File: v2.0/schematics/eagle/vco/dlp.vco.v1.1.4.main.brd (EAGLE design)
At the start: 87.9 x 38.1 mm, 72 parts, among them IC1 TL074P, IC2 TL074P, IC3 TL074P, IC5 TL072P, Q1 2N4401, Q10 2N4401, Q2 2N4401, Q3 2N3417, Q4 2N3906, Q5 2N3417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

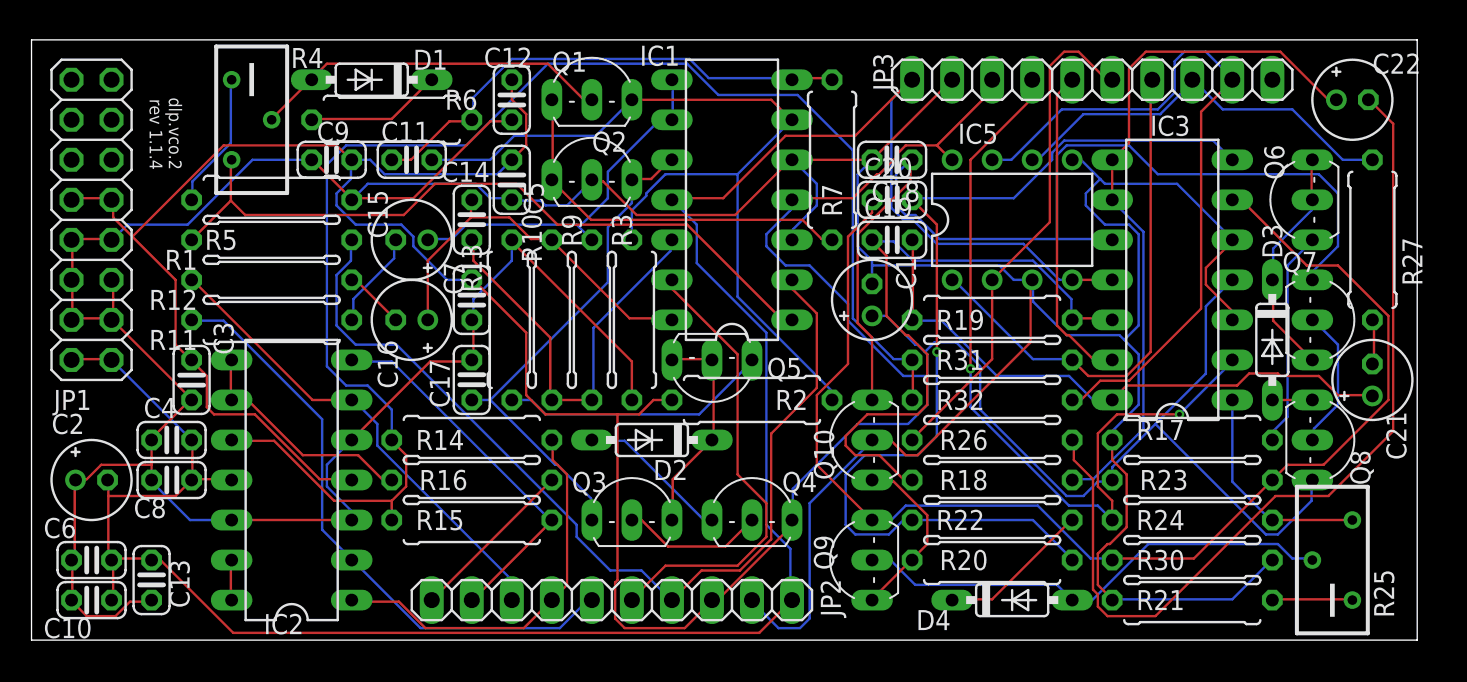
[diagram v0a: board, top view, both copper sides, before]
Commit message: Update component names on board layout Reverse cap polarity on v1.0 psu schem
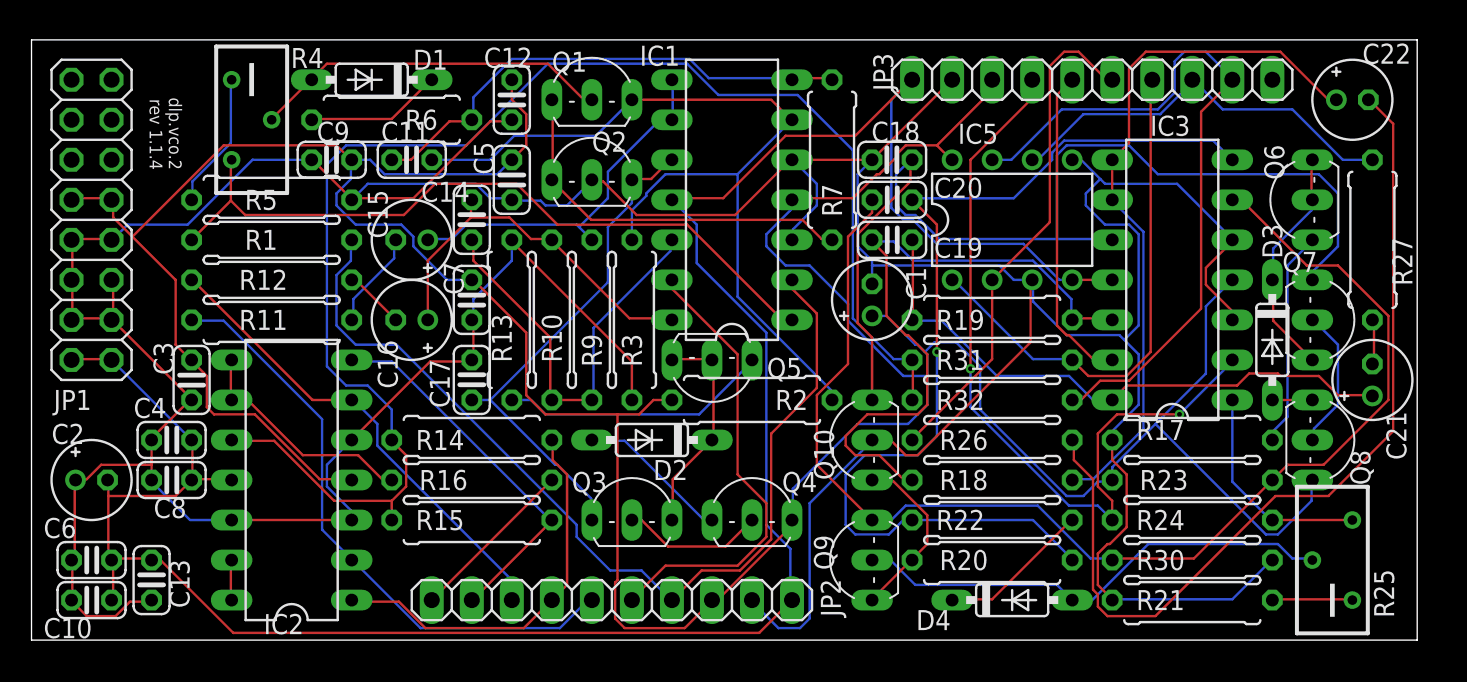
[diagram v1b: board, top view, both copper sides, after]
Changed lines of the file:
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@@
 </element>
 <element name="C5" library="_common" package="C025-024X044" value="0.1uF" x="30.48" y="29.21" smashed="yes" rot="R270">
-<attribute name="NAME" x="31.242" y="29.083" size="1.27" layer="25" ratio="10" rot="R270"/>
+<attribute name="NAME" x="28.067" y="31.623" size="1.27" layer="25" ratio="10" rot="R270"/>
 <attribute name="VALUE" x="27.813" y="30.988" size="1.27" layer="27" ratio="10" rot="R270"/>
 </element>
@@
 </element>
 <element name="C3" library="_common" package="C025-024X044" value="0.1uF" x="10.16" y="16.51" smashed="yes" rot="R270">
-<attribute name="NAME" x="11.557" y="20.193" size="1.27" layer="25" ratio="10" rot="R270"/>
+<attribute name="NAME" x="7.747" y="18.923" size="1.27" layer="25" ratio="10" rot="R270"/>
 <attribute name="VALUE" x="7.493" y="18.288" size="1.27" layer="27" ratio="10" rot="R270"/>
 </element>
 <element name="C1" library="_common" package="E2-5" value="10uF" x="53.34" y="21.59" smashed="yes" rot="R90">
-<attribute name="NAME" x="56.134" y="22.225" size="1.27" layer="25" ratio="10" rot="R90"/>
+<attribute name="NAME" x="56.769" y="21.59" size="1.27" layer="25" ratio="10" rot="R90"/>
 <attribute name="VALUE" x="55.499" y="24.13" size="1.27" layer="27" ratio="10" rot="R90"/>
 </element>
 <element name="C14" library="_common" package="C025-024X044" value="18pF" x="27.94" y="26.67" smashed="yes" rot="R90">
-<attribute name="NAME" x="29.083" y="30.353" size="1.27" layer="25" ratio="10" rot="R180"/>
+<attribute name="NAME" x="27.813" y="29.083" size="1.27" layer="25" ratio="10" rot="R180"/>
 <attribute name="VALUE" x="30.607" y="24.892" size="1.27" layer="27" ratio="10" rot="R90"/>
 </element>
@@
 </element>
 <element name="C8" library="_common" package="C025-024X044" value="0.1uF" x="8.89" y="10.16" smashed="yes">
-<attribute name="NAME" x="6.477" y="7.747" size="1.27" layer="25" ratio="10"/>
+<attribute name="NAME" x="7.747" y="7.747" size="1.27" layer="25" ratio="10"/>
 <attribute name="VALUE" x="7.112" y="7.493" size="1.27" layer="27" ratio="10"/>
 </element>
@@
 </element>
 <element name="C4" library="_common" package="C025-024X044" value="0.1uF" x="8.89" y="12.7" smashed="yes">
-<attribute name="NAME" x="7.112" y="14.097" size="1.27" layer="25" ratio="10"/>
+<attribute name="NAME" x="6.477" y="14.097" size="1.27" layer="25" ratio="10"/>
 <attribute name="VALUE" x="7.112" y="10.033" size="1.27" layer="27" ratio="10"/>
 </element>
 <element name="C2" library="_common" package="E2-5" value="10uF" x="3.81" y="10.16" smashed="yes">
-<attribute name="NAME" x="1.27" y="13.081" size="1.27" layer="25" ratio="10"/>
+<attribute name="NAME" x="1.27" y="12.446" size="1.27" layer="25" ratio="10"/>
 <attribute name="VALUE" x="6.35" y="8.001" size="1.27" layer="27" ratio="10"/>
 </element>
@@
 </element>
 <element name="R13" library="_common" package="0309/10" value="10K" x="30.48" y="20.32" smashed="yes" rot="R270">
-<attribute name="NAME" x="27.305" y="25.146" size="1.27" layer="25" ratio="10" rot="R270"/>
+<attribute name="NAME" x="29.21" y="20.701" size="1.27" layer="25" ratio="10" rot="R270"/>
 <attribute name="VALUE" x="29.7942" y="23.495" size="1.27" layer="27" ratio="10" rot="R270"/>
 </element>
@@
 </element>
 <element name="R1" library="_common" package="0309/10" value="2.2K" x="15.24" y="25.4" smashed="yes" rot="R180">
-<attribute name="NAME" x="10.541" y="24.765" size="1.27" layer="25" ratio="10" rot="R180"/>
+<attribute name="NAME" x="15.621" y="26.035" size="1.27" layer="25" ratio="10" rot="R180"/>
 <attribute name="VALUE" x="18.415" y="26.0858" size="1.27" layer="27" ratio="10" rot="R180"/>
 </element>
 <element name="R11" library="_common" package="0309/10" value="22K" x="15.24" y="20.32" smashed="yes" rot="R180">
-<attribute name="NAME" x="10.541" y="19.685" size="1.27" layer="25" ratio="10" rot="R180"/>
+<attribute name="NAME" x="16.256" y="20.955" size="1.27" layer="25" ratio="10" rot="R180"/>
 <attribute name="VALUE" x="18.415" y="21.0058" size="1.27" layer="27" ratio="10" rot="R180"/>
 </element>
 <element name="R12" library="_common" package="0309/10" value="22K" x="15.24" y="22.86" smashed="yes" rot="R180">
-<attribute name="NAME" x="10.541" y="22.225" size="1.27" layer="25" ratio="10" rot="R180"/>
+<attribute name="NAME" x="16.256" y="23.495" size="1.27" layer="25" ratio="10" rot="R180"/>
 <attribute name="VALUE" x="18.415" y="23.5458" size="1.27" layer="27" ratio="10" rot="R180"/>
 </element>
 <element name="R9" library="_common" package="0309/10" value="100K" x="35.56" y="20.32" smashed="yes" rot="R270">
-<attribute name="NAME" x="33.655" y="27.051" size="1.27" layer="25" ratio="10" rot="R270"/>
+<attribute name="NAME" x="34.925" y="19.431" size="1.27" layer="25" ratio="10" rot="R270"/>
 <attribute name="VALUE" x="34.8742" y="23.495" size="1.27" layer="27" ratio="10" rot="R270"/>
 </element>
 <element name="R10" library="_common" package="0309/10" value="3.3M" x="33.02" y="20.32" smashed="yes" rot="R270">
-<attribute name="NAME" x="31.115" y="27.051" size="1.27" layer="25" ratio="10" rot="R270"/>
+<attribute name="NAME" x="32.385" y="20.701" size="1.27" layer="25" ratio="10" rot="R270"/>
 <attribute name="VALUE" x="32.3342" y="23.495" size="1.27" layer="27" ratio="10" rot="R270"/>
 </element>
@@
 </element>
 <element name="R3" library="_common" package="0309/10" value="100K" x="38.1" y="20.32" smashed="yes" rot="R270">
-<attribute name="NAME" x="36.83" y="27.051" size="1.27" layer="25" ratio="10" rot="R270"/>
+<attribute name="NAME" x="37.465" y="19.431" size="1.27" layer="25" ratio="10" rot="R270"/>
 <attribute name="VALUE" x="37.4142" y="23.495" size="1.27" layer="27" ratio="10" rot="R270"/>
 </element>
@@
 </element>
 <element name="R5" library="_common" package="0309/10" value="390" x="15.24" y="27.94" smashed="yes" rot="R180">
-<attribute name="NAME" x="13.081" y="26.035" size="1.27" layer="25" ratio="10" rot="R180"/>
+<attribute name="NAME" x="15.621" y="28.575" size="1.27" layer="25" ratio="10" rot="R180"/>
 <attribute name="VALUE" x="18.415" y="28.6258" size="1.27" layer="27" ratio="10" rot="R180"/>
 </element>
 <element name="R6" library="_common" package="0309/10" value="220K" x="22.86" y="33.02" smashed="yes" rot="R180">
-<attribute name="NAME" x="28.321" y="34.925" size="1.27" layer="25" ratio="10" rot="R180"/>
+<attribute name="NAME" x="25.781" y="33.655" size="1.27" layer="25" ratio="10" rot="R180"/>
 <attribute name="VALUE" x="26.035" y="33.7058" size="1.27" layer="27" ratio="10" rot="R180"/>
 </element>
@@
 </element>
 <element name="C18" library="_common" package="C025-024X044" value="0.01uF" x="54.61" y="30.48" smashed="yes" rot="R180">
-<attribute name="NAME" x="56.388" y="29.083" size="1.27" layer="25" ratio="10" rot="R180"/>
+<attribute name="NAME" x="56.388" y="32.893" size="1.27" layer="25" ratio="10" rot="R180"/>
 <attribute name="VALUE" x="56.388" y="33.147" size="1.27" layer="27" ratio="10" rot="R180"/>
 </element>
@@
 </element>
 <element name="C19" library="_common" package="C025-024X044" value="18pF" x="54.61" y="25.4" smashed="yes">
-<attribute name="NAME" x="52.832" y="26.797" size="1.27" layer="25" ratio="10"/>
+<attribute name="NAME" x="57.277" y="24.257" size="1.27" layer="25" ratio="10"/>
 <attribute name="VALUE" x="52.832" y="22.733" size="1.27" layer="27" ratio="10"/>
 </element>
@@
 </element>
 <element name="C20" library="_common" package="C025-024X044" value="100pF" x="54.61" y="27.94" smashed="yes">
-<attribute name="NAME" x="52.832" y="29.337" size="1.27" layer="25" ratio="10"/>
+<attribute name="NAME" x="57.277" y="28.067" size="1.27" layer="25" ratio="10"/>
 <attribute name="VALUE" x="52.832" y="25.273" size="1.27" layer="27" ratio="10"/>
 </element>
@@
 </element>
 <element name="C22" library="_common" package="E2-5" value="10uF" x="83.82" y="34.29" smashed="yes">
-<attribute name="NAME" x="85.09" y="35.941" size="1.27" layer="25" ratio="10"/>
+<attribute name="NAME" x="84.455" y="36.576" size="1.27" layer="25" ratio="10"/>
 <attribute name="VALUE" x="86.36" y="32.131" size="1.27" layer="27" ratio="10"/>
 </element>
@@
 </element>
 <element name="R27" library="_common" package="0309/10" value="22K" x="85.09" y="25.4" smashed="yes" rot="R90">
-<attribute name="NAME" x="88.265" y="22.479" size="1.27" layer="25" ratio="10" rot="R90"/>
+<attribute name="NAME" x="87.63" y="22.479" size="1.27" layer="25" ratio="10" rot="R90"/>
 <attribute name="VALUE" x="85.7758" y="22.225" size="1.27" layer="27" ratio="10" rot="R90"/>
 </element>
